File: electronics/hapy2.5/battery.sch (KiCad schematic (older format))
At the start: 39 parts, among them Q3 BD140, Q4 2N7002, Q5 BSS84P H6327, U3 DCDC_TI_TPS54335A, U5 LM317

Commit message: double check all component to footprint matches
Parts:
- D14, D7: footprint Diodes_SMD:SOD-123 -> risebox:DIODE_SOD-123
- Q4, Q5: footprint corecode:SOT-23-FET -> risebox:SOT-23-FET
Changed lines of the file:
@@
 F 0 "D7" H 3600 3500 50  0000 C CNN
 F 1 "MMSZ4701-E3-08 ZENER" H 3600 3300 40  0000 C CNN
-F 2 "Diodes_SMD:SOD-123" H 3600 3400 60  0001 C CNN
+F 2 "risebox:DIODE_SOD-123" H 3600 3400 60  0001 C CNN
 F 3 "" H 3600 3400 60  0000 C CNN
 	1    3600 3400
@@
 F 0 "Q5" H 4600 5190 60  0000 R CNN
 F 1 "BSS84P H6327" H 4600 4820 60  0000 R CNN
-F 2 "corecode:SOT-23-FET" H 4600 5000 60  0001 C CNN
+F 2 "risebox:SOT-23-FET" H 4600 5000 60  0001 C CNN
 F 3 "" H 4600 5000 60  0000 C CNN
 	1    4600 5000
@@
 F 0 "Q4" H 4260 6620 60  0000 R CNN
 F 1 "2N7002" H 4260 6300 60  0000 R CNN
-F 2 "corecode:SOT-23-FET" H 4250 6450 60  0001 C CNN
+F 2 "risebox:SOT-23-FET" H 4250 6450 60  0001 C CNN
 F 3 "" H 4250 6450 60  0000 C CNN
 	1    4250 6450
@@
 F 0 "D14" H 5350 2200 50  0000 C CNN
 F 1 "MMSZ4678T1G  ZENER" H 5350 2000 40  0000 C CNN
-F 2 "Diodes_SMD:SOD-123" H 5350 2100 60  0001 C CNN
+F 2 "risebox:DIODE_SOD-123" H 5350 2100 60  0001 C CNN
 F 3 "" H 5350 2100 60  0000 C CNN
 	1    5350 2100

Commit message: routing P8 in progress
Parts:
- BT1: footprint Connect:bornier2 -> smisioto_bornier_mpt:mpt_0,5%2f2-2,54
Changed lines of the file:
@@
 F 0 "BT1" H 1150 3300 50  0000 C CNN
 F 1 "BATTERY" H 1150 2910 50  0000 C CNN
-F 2 "Connect:bornier2" H 1150 3100 60  0001 C CNN
+F 2 "smisioto_bornier_mpt:mpt_0,5%2f2-2,54" H 1150 3100 60  0001 C CNN
 F 3 "" H 1150 3100 60  0000 C CNN
 	1    1150 3100

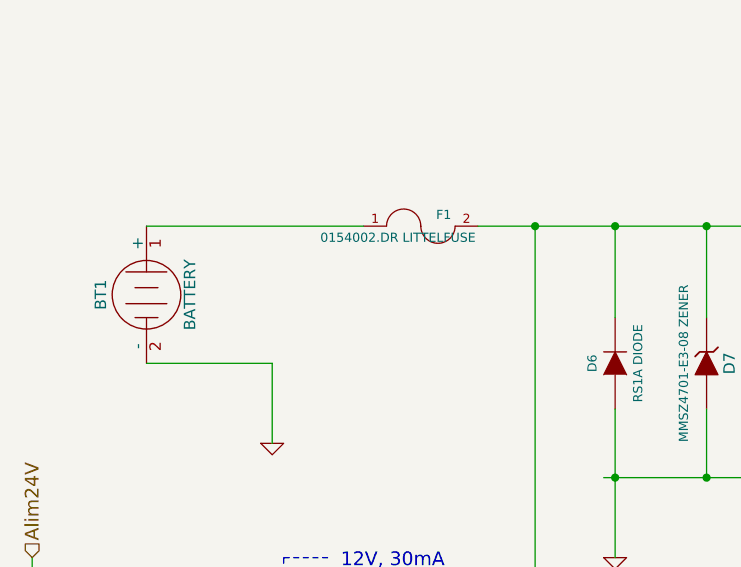
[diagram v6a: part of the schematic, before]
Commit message: 2nd dcdc and charger circuit done
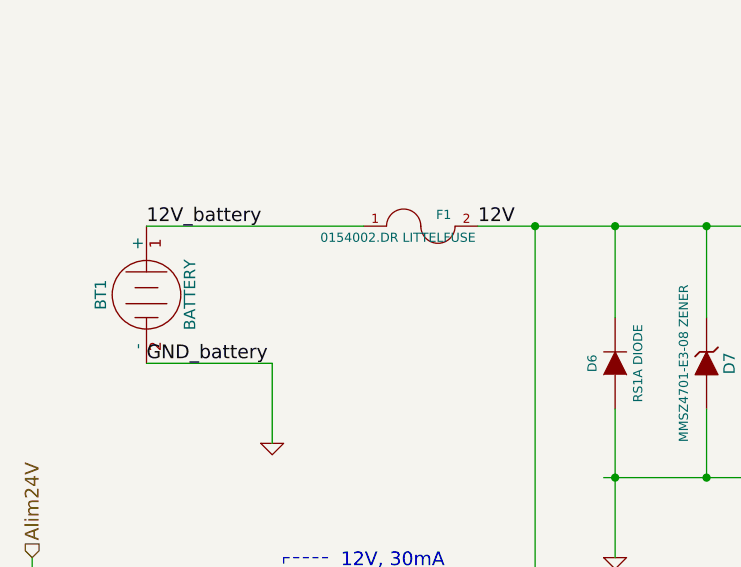
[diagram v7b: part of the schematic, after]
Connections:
- net 12V: now reaches C10.1, C11.1, C12.1, D6.2 (K), D7.2 (K), F1.2, Q3.1 (E), Q5.D, R44.1, R47.2, U3.2 (VIN)
- net 12V_battery: now reaches BT1.1 (+), F1.1
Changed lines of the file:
@@
 	1    0    0    -1
 $EndComp
+Text Label 1150 2800 0    60   ~ 0
+12V_battery
+Text Label 1150 3400 0    60   ~ 0
+GND_battery
+Text Label 2600 2800 0    60   ~ 0
+12V
 $EndSCHEMATC

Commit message: gerbers plus repaired pcb
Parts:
- R38: value 36K -> 9.76K
- R39: value 5K -> 1K
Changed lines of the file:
@@
 P 1600 5350
 F 0 "R39" V 1680 5350 40  0000 C CNN
-F 1 "5K" V 1607 5351 40  0000 C CNN
+F 1 "1K" V 1607 5351 40  0000 C CNN
 F 2 "Resistors_SMD:R_0603" V 1530 5350 30  0001 C CNN
 F 3 "" H 1600 5350 30  0000 C CNN
@@
 P 1050 6150
 F 0 "R38" V 1130 6150 40  0000 C CNN
-F 1 "36K" V 1057 6151 40  0000 C CNN
+F 1 "9.76K" V 1057 6151 40  0000 C CNN
 F 2 "Resistors_SMD:R_0603" V 980 6150 30  0001 C CNN
 F 3 "" H 1050 6150 30  0000 C CNN
